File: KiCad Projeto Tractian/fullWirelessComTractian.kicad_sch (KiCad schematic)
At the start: 28 parts, among them U1 ESP8266EX, U2 MX25R3235FM2xx1, U4 MX25R3235FM2xx1, U5 AMS1117-3.3, U6 TMP36xS, Y2 XTAL 16Mhz ±10ppm (TSX -3225 )

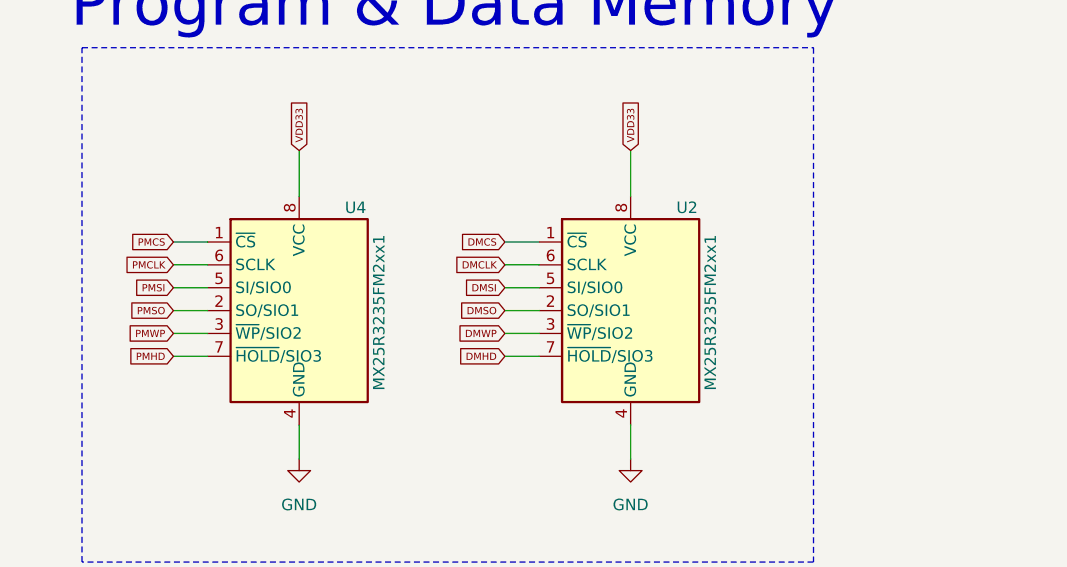
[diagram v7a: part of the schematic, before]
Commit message: :bug: fix da Read subroutine
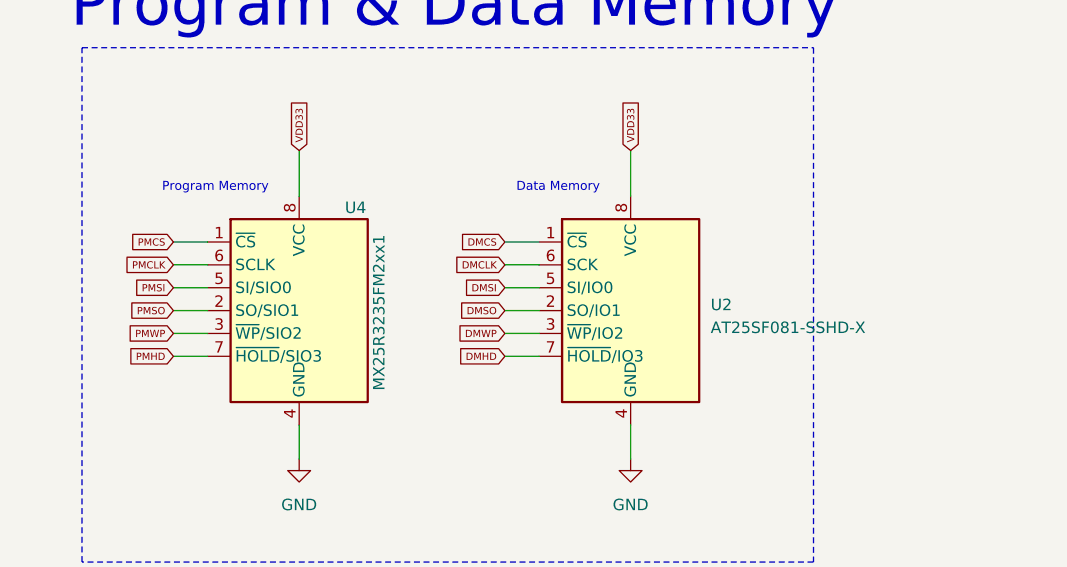
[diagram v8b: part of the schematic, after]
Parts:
- removed U2: MX25R3235FM2xx1, Package_SO:SOP-8_5.28x5.23mm_P1.27mm, symbol Memory_Flash:MX25R3235FM2xx1
- added U2: AT25SF081-SSHD-X, Package_SO:SOIC-8_3.9x4.9mm_P1.27mm, symbol Memory_Flash:AT25SF081-SSHD-X
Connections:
- net DMCLK: now also U2.6 (SCK)
- net DMCS: now also U2.1 (~{CS})
- net DMHD: now also U2.7 (~{HOLD}/IO3)
- net DMSI: now also U2.5 (SI/IO0)
- net DMSO: now also U2.2 (SO/IO1)
- net DMWP: now also U2.3 (~{WP}/IO2)
- net GND: now also U2.4 (GND)
- net VDD33: now also U2.8 (VCC)
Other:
- note added: "Data Memory"
- note added: "Program Memory"
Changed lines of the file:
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@@
     (effects (font (size 5 5)) (justify left bottom))
+  )
+  (text "Program Memory\n\n" (at 199.39 40.64 0)
+    (effects (font (size 1 1)) (justify left bottom))
+  )
+  (text "Data Memory\n\n" (at 238.76 40.64 0)
+    (effects (font (size 1 1)) (justify left bottom))
   )
   (text "Main circuitry" (at 15.24 81.28 0)
@@
     )
   )
-  (symbol (lib_id "power:GND") (at 27.94 142.24 0) (unit 1)
-    (in_bom yes) (on_board yes) (dnp no) (fields_autoplaced)
-    (property "Reference" "#PWR019" (at 27.94 148.59 0)
-      (effects (font (size 1.27 1.27)) hide)
-    )
-    (property "Value" "GND" (at 27.94 147.32 0)
-      (effects (font (size 1.27 1.27)))
-    )
-    (property "Footprint" "" (at 27.94 142.24 0)
-      (effects (font (size 1.27 1.27)) hide)
-    )
-    (property "Datasheet" "" (at 27.94 142.24 0)
-      (effects (font (size 1.27 1.27)) hide)
-    )
-    (pin "1")
-    (instances
-      (project "fullWirelessComTractian"
-        (path "/de37416f-2273-481a-bd7e-d92c2e99b78a"
-          (reference "#PWR019") (unit 1)
-        )
-      )
-    )
-  )
-  (symbol (lib_id "Device:C") (at 69.85 172.72 0) (mirror y) (unit 1)
-    (in_bom yes) (on_board yes) (dnp no) (fields_autoplaced)
-    (property "Reference" "C11" (at 73.66 172.085 0)
-      (effects (font (size 1.27 1.27)) (justify right))
-    )
-    (property "Value" "15pF" (at 73.66 174.625 0)
-      (effects (font (size 1.27 1.27)) (justify right))
-    )
-    (property "Footprint" "Capacitor_SMD:C_0201_0603Metric_Pad0.64x0.40mm_HandSolder" (at 68.8848 176.53 0)
-      (effects (font (size 1.27 1.27)) hide)
-    )
-    (property "Datasheet" "~" (at 69.85 172.72 0)
-      (effects (font (size 1.27 1.27)) hide)
-    )
-    (pin "1")
-    (pin "2")
-    (instances
-      (project "fullWirelessComTractian"
-        (path "/de37416f-2273-481a-bd7e-d92c2e99b78a"
-          (reference "C11") (unit 1)
-        )
-      )
-    )
-  )
-  (symbol (lib_id "power:GND") (at 229.87 144.78 0) (unit 1)
-    (in_bom yes) (on_board yes) (dnp no) (fields_autoplaced)
-    (property "Reference" "#PWR02" (at 229.87 151.13 0)
-      (effects (font (size 1.27 1.27)) hide)
-    )
-    (property "Value" "GND" (at 229.87 149.86 0)
-      (effects (font (size 1.27 1.27)))
-    )
-    (property "Footprint" "" (at 229.87 144.78 0)
-      (effects (font (size 1.27 1.27)) hide)
-    )
-    (property "Datasheet" "" (at 229.87 144.78 0)
-      (effects (font (size 1.27 1.27)) hide)
-    )
-    (pin "1")
-    (instances
-      (project "fullWirelessComTractian"
-        (path "/de37416f-2273-481a-bd7e-d92c2e99b78a"
-          (reference "#PWR02") (unit 1)
-        )
-      )
-    )
-  )
-  (symbol (lib_id "Sensor_Temperature:TMP36xS") (at 229.87 130.81 0) (unit 1)
-    (in_bom yes) (on_board yes) (dnp no)
-    (property "Reference" "U6" (at 233.68 121.92 0)
-      (effects (font (size 1.27 1.27)))
-    )
-    (property "Value" "TMP36xS" (at 236.22 139.7 0)
-      (effects (font (size 1.27 1.27)))
-    )
-    (property "Footprint" "Package_SO:SOIC-8_3.9x4.9mm_P1.27mm" (at 229.87 142.24 0)
-      (effects (font (size 1.27 1.27)) hide)
-    )
-    (property "Datasheet" "https://www.analog.com/media/en/technical-documentation/data-sheets/TMP35_36_37.pdf" (at 229.87 130.81 0)
-      (effects (font (size 1.27 1.27)) hide)
-    )
-    (pin "1")
-    (pin "4")
-    (pin "5")
-    (pin "8")
-    (instances
-      (project "fullWirelessComTractian"
-        (path "/de37416f-2273-481a-bd7e-d92c2e99b78a"
-          (reference "U6") (unit 1)
-        )
-      )
-    )
-  )
-  (symbol (lib_id "Memory_Flash:MX25R3235FM2xx1") (at 251.46 52.07 0) (unit 1)
-    (in_bom yes) (on_board yes) (dnp no)
-    (property "Reference" "U2" (at 256.54 40.64 0)
+  (symbol (lib_id "Memory_Flash:AT25SF081-SSHD-X") (at 251.46 52.07 0) (unit 1)
+    (in_bom yes) (on_board yes) (dnp no) (fields_autoplaced)
+    (property "Reference" "U2" (at 260.35 51.435 0)
       (effects (font (size 1.27 1.27)) (justify left))
     )
-    (property "Value" "MX25R3235FM2xx1" (at 260.35 60.96 90)
+    (property "Value" "AT25SF081-SSHD-X" (at 260.35 53.975 0)
       (effects (font (size 1.27 1.27)) (justify left))
     )
-    (property "Footprint" "Package_SO:SOP-8_5.28x5.23mm_P1.27mm" (at 251.46 67.31 0)
-      (effects (font (size 1.27 1.27)) hide)
-    )
-    (property "Datasheet" "http://www.macronix.com/Lists/Datasheet/Attachments/7534/MX25R3235F,%20Wide%20Range,%2032Mb,%20v1.6.pdf" (at 251.46 52.07 0)
+    (property "Footprint" "Package_SO:SOIC-8_3.9x4.9mm_P1.27mm" (at 251.46 67.31 0)
+      (effects (font (size 1.27 1.27)) hide)
+    )
+    (property "Datasheet" "https://www.adestotech.com/wp-content/uploads/DS-AT25SF081_045.pdf" (at 251.46 52.07 0)
       (effects (font (size 1.27 1.27)) hide)
     )
@@
         )
       )
+    )
+  )
+  (symbol (lib_id "power:GND") (at 27.94 142.24 0) (unit 1)
+    (in_bom yes) (on_board yes) (dnp no) (fields_autoplaced)
+    (property "Reference" "#PWR019" (at 27.94 148.59 0)
+      (effects (font (size 1.27 1.27)) hide)
+    )
+    (property "Value" "GND" (at 27.94 147.32 0)
+      (effects (font (size 1.27 1.27)))
+    )
+    (property "Footprint" "" (at 27.94 142.24 0)
+      (effects (font (size 1.27 1.27)) hide)
+    )
+    (property "Datasheet" "" (at 27.94 142.24 0)
+      (effects (font (size 1.27 1.27)) hide)
+    )
+    (pin "1")
+    (instances
+      (project "fullWirelessComTractian"
+        (path "/de37416f-2273-481a-bd7e-d92c2e99b78a"
+          (reference "#PWR019") (unit 1)
+        )
+      )
+    )
+  )
+  (symbol (lib_id "Device:C") (at 69.85 172.72 0) (mirror y) (unit 1)
+    (in_bom yes) (on_board yes) (dnp no) (fields_autoplaced)
+    (property "Reference" "C11" (at 73.66 172.085 0)
+      (effects (font (size 1.27 1.27)) (justify right))
+    )
+    (property "Value" "15pF" (at 73.66 174.625 0)
+      (effects (font (size 1.27 1.27)) (justify right))
+    )
+    (property "Footprint" "Capacitor_SMD:C_0201_0603Metric_Pad0.64x0.40mm_HandSolder" (at 68.8848 176.53 0)
+      (effects (font (size 1.27 1.27)) hide)
+    )
+    (property "Datasheet" "~" (at 69.85 172.72 0)
+      (effects (font (size 1.27 1.27)) hide)
+    )
+    (pin "1")
+    (pin "2")
+    (instances
+      (project "fullWirelessComTractian"
+        (path "/de37416f-2273-481a-bd7e-d92c2e99b78a"
+          (reference "C11") (unit 1)
+        )
+      )
+    )
+  )
+  (symbol (lib_id "power:GND") (at 229.87 144.78 0) (unit 1)
+    (in_bom yes) (on_board yes) (dnp no) (fields_autoplaced)
+    (property "Reference" "#PWR02" (at 229.87 151.13 0)
+      (effects (font (size 1.27 1.27)) hide)
+    )
+    (property "Value" "GND" (at 229.87 149.86 0)
+      (effects (font (size 1.27 1.27)))
+    )
+    (property "Footprint" "" (at 229.87 144.78 0)
+      (effects (font (size 1.27 1.27)) hide)
+    )
+    (property "Datasheet" "" (at 229.87 144.78 0)
+      (effects (font (size 1.27 1.27)) hide)
+    )
+    (pin "1")
+    (instances
+      (project "fullWirelessComTractian"
+        (path "/de37416f-2273-481a-bd7e-d92c2e99b78a"
+          (reference "#PWR02") (unit 1)
+        )
+      )
+    )
+  )
+  (symbol (lib_id "Sensor_Temperature:TMP36xS") (at 229.87 130.81 0) (unit 1)
+    (in_bom yes) (on_board yes) (dnp no)
+    (property "Reference" "U6" (at 233.68 121.92 0)
+      (effects (font (size 1.27 1.27)))
+    )
+    (property "Value" "TMP36xS" (at 236.22 139.7 0)
+      (effects (font (size 1.27 1.27)))
+    )
+    (property "Footprint" "Package_SO:SOIC-8_3.9x4.9mm_P1.27mm" (at 229.87 142.24 0)
+      (effects (font (size 1.27 1.27)) hide)
+    )
+    (property "Datasheet" "https://www.analog.com/media/en/technical-documentation/data-sheets/TMP35_36_37.pdf" (at 229.87 130.81 0)
+      (effects (font (size 1.27 1.27)) hide)
+    )
+    (pin "1")
+    (pin "4")
+    (pin "5")
+    (pin "8")
+    (instances
+      (project "fullWirelessComTractian"
+        (path "/de37416f-2273-481a-bd7e-d92c2e99b78a"
+          (reference "U6") (unit 1)
+        )
+      )
